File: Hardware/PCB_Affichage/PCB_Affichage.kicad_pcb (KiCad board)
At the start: 2 copper layers, 41 x 28 mm, 8 parts, among them J1 Conn_01x02, J2 Conn_01x03

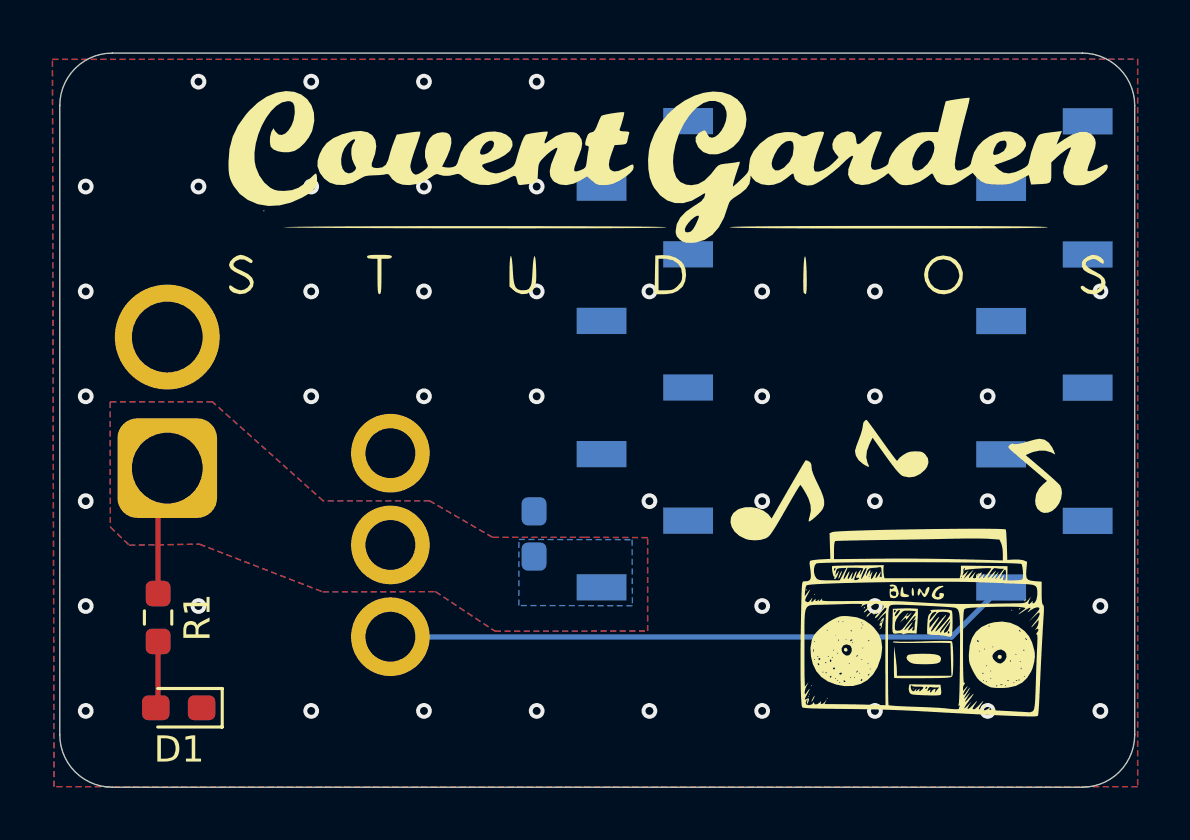
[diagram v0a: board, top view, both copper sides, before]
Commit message: ajout des pinheaders en plus
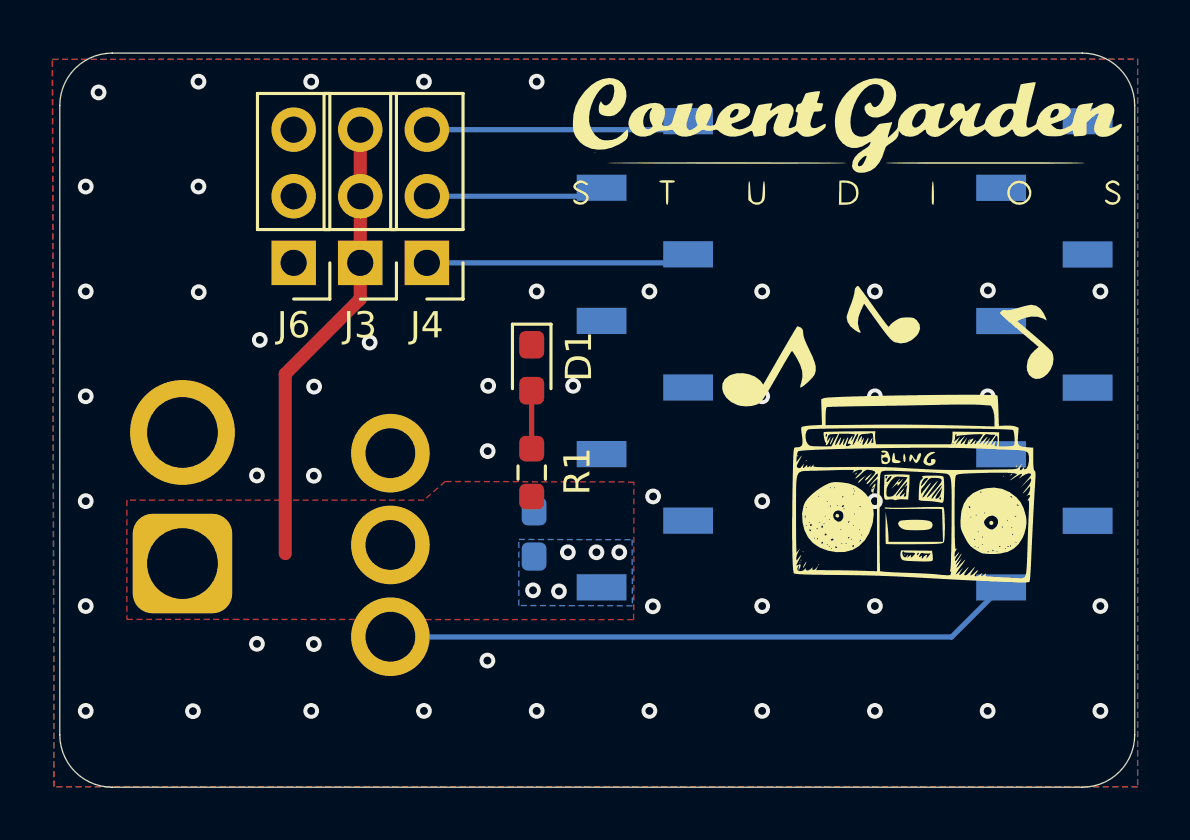
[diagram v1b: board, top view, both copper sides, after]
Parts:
- removed the G*** at (110.3, 51.7)
- added G***: LOGO, img:logo_covent_petit, F.Cu at (117.1, 49.6)
- added J3: Conn_01x03, Connector_PinHeader_2.54mm:PinHeader_1x03_P2.54mm_Vertical, F.Cu at (98.5, 54.0)
- added J4: Conn_01x03, Connector_PinHeader_2.54mm:PinHeader_1x03_P2.54mm_Vertical, F.Cu at (101.0, 54.0)
- added J6: Conn_01x03, Connector_PinHeader_2.54mm:PinHeader_1x03_P2.54mm_Vertical, F.Cu at (95.9, 54.0)
- moved D1 18.7 mm to (105.0, 58.0), turned to -90 degrees
- moved R1 15.3 mm to (105.0, 62.0), turned to 90 degrees
- moved G*** 5.12 mm to (119.0, 60.8)
- moved J1 3.69 mm to (91.7, 65.5)
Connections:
- U2 pad 1: unconnected-(U2-GPIO0-Pad1) -> /GPIO1
- U2 pad 2: unconnected-(U2-GPIO1-Pad2) -> /GPIO2
- U2 pad 3: unconnected-(U2-GPIO2-Pad3) -> /GPIO3
- U2 pad 4: unconnected-(U2-GPIO3-Pad4) -> /GPIO4
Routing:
- net +5V: track 4.93 -> 17.4 mm, vias 0 -> 5
- net /GPIO3: track 0.00 -> 10.1 mm
- net /GPIO1: track 0.00 -> 10.1 mm
- net /GPIO2: track 0.00 -> 6.80 mm
- net GND: vias 43 -> 50
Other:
- board text added: "5V"
- board text added: "Gnd"
- board text added: "IO"

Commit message: correction orientation des connecteurs sur secteur
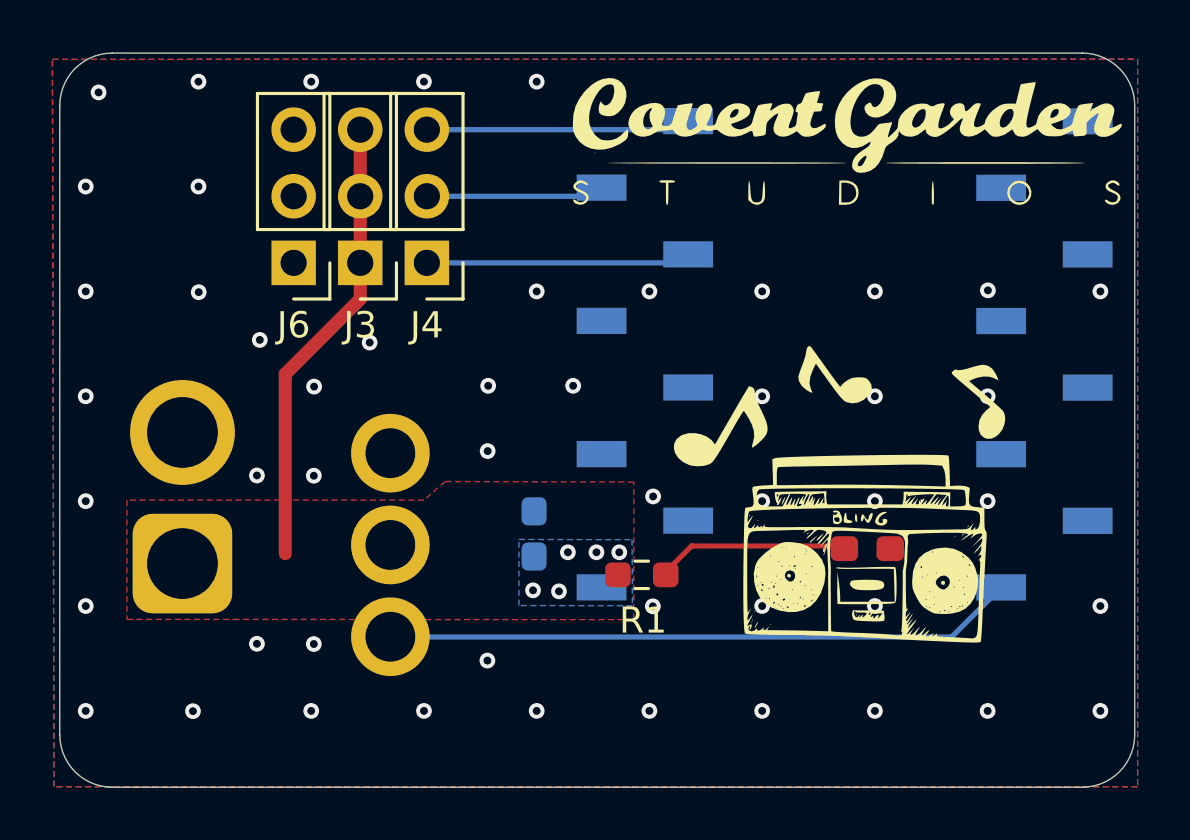
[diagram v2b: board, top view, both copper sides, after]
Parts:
- removed the G*** at (119.0, 60.8)
- D1: footprint LED_SMD:LED_0603_1608Metric_Pad1.05x0.95mm_HandSolder -> img:LED_0603_avec_dessin
- moved D1 14.7 mm to (117.8, 65.3), turned to 0 degrees
- moved R1 5.73 mm to (109.2, 65.9), turned to 0 degrees
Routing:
- net Net-(D1-A): track 2.21 -> 7.38 mm
